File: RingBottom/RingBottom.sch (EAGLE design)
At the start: 28 parts

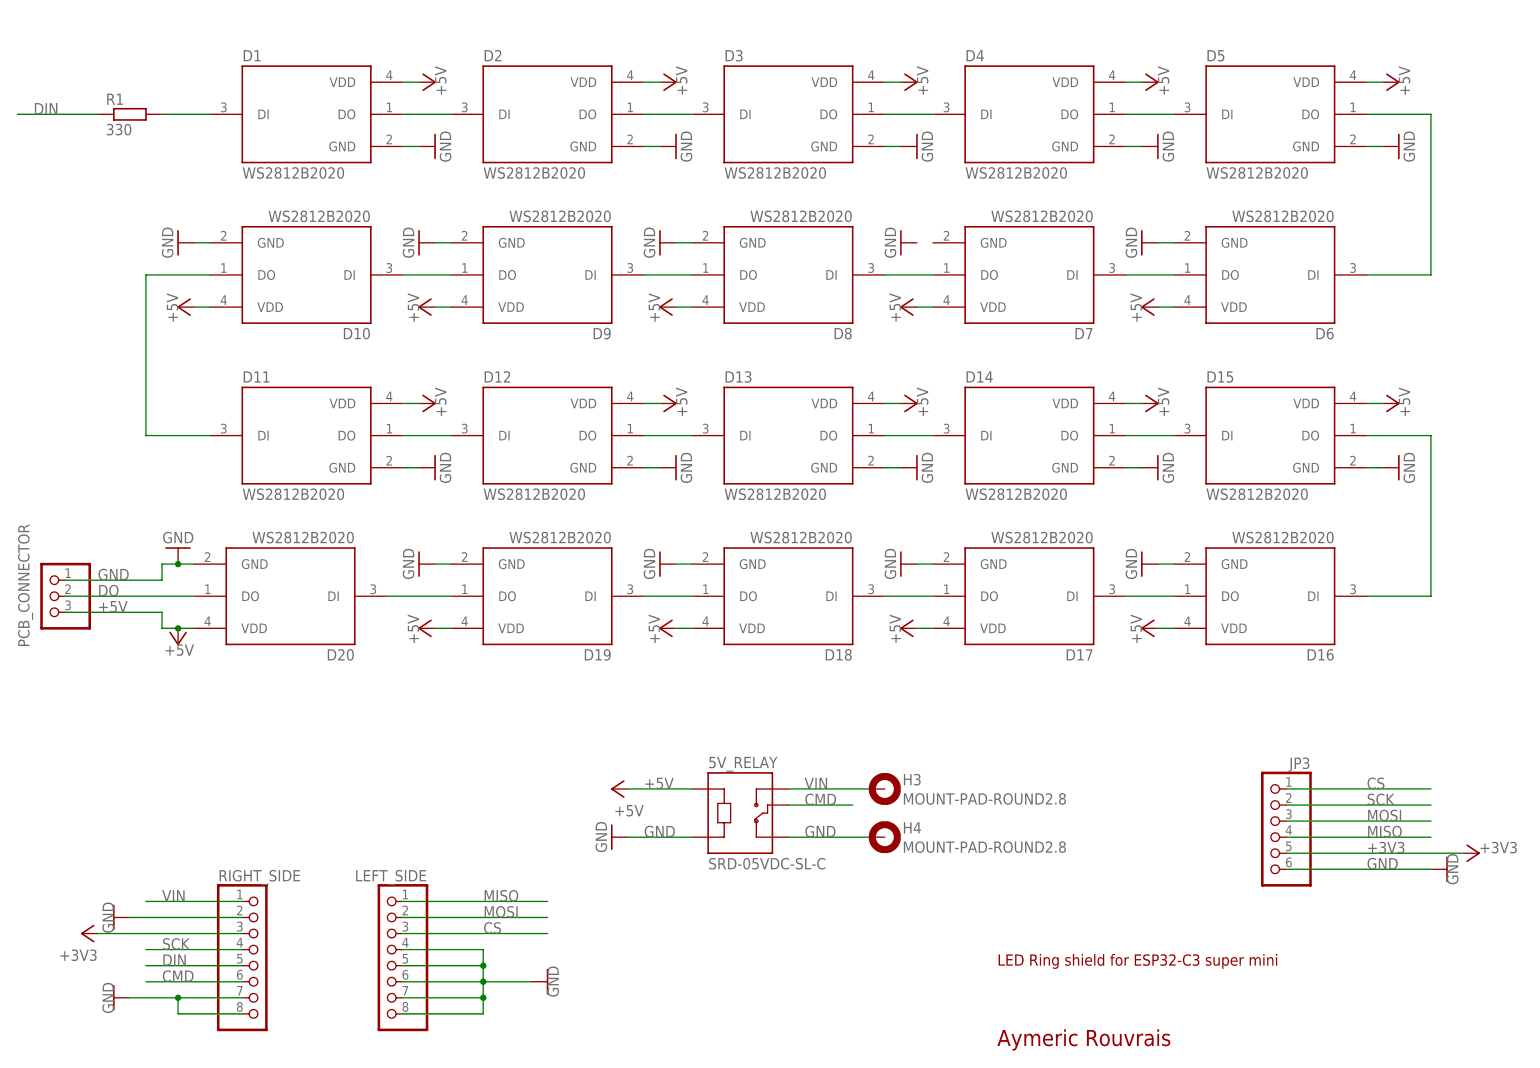
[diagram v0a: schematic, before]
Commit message: V2.0
Now there is a top and bottom PCB. They have the correct dimensions.
The bottom one has the LEDs and the top one has all the rest.
There is still a possibility to integrate a sd card
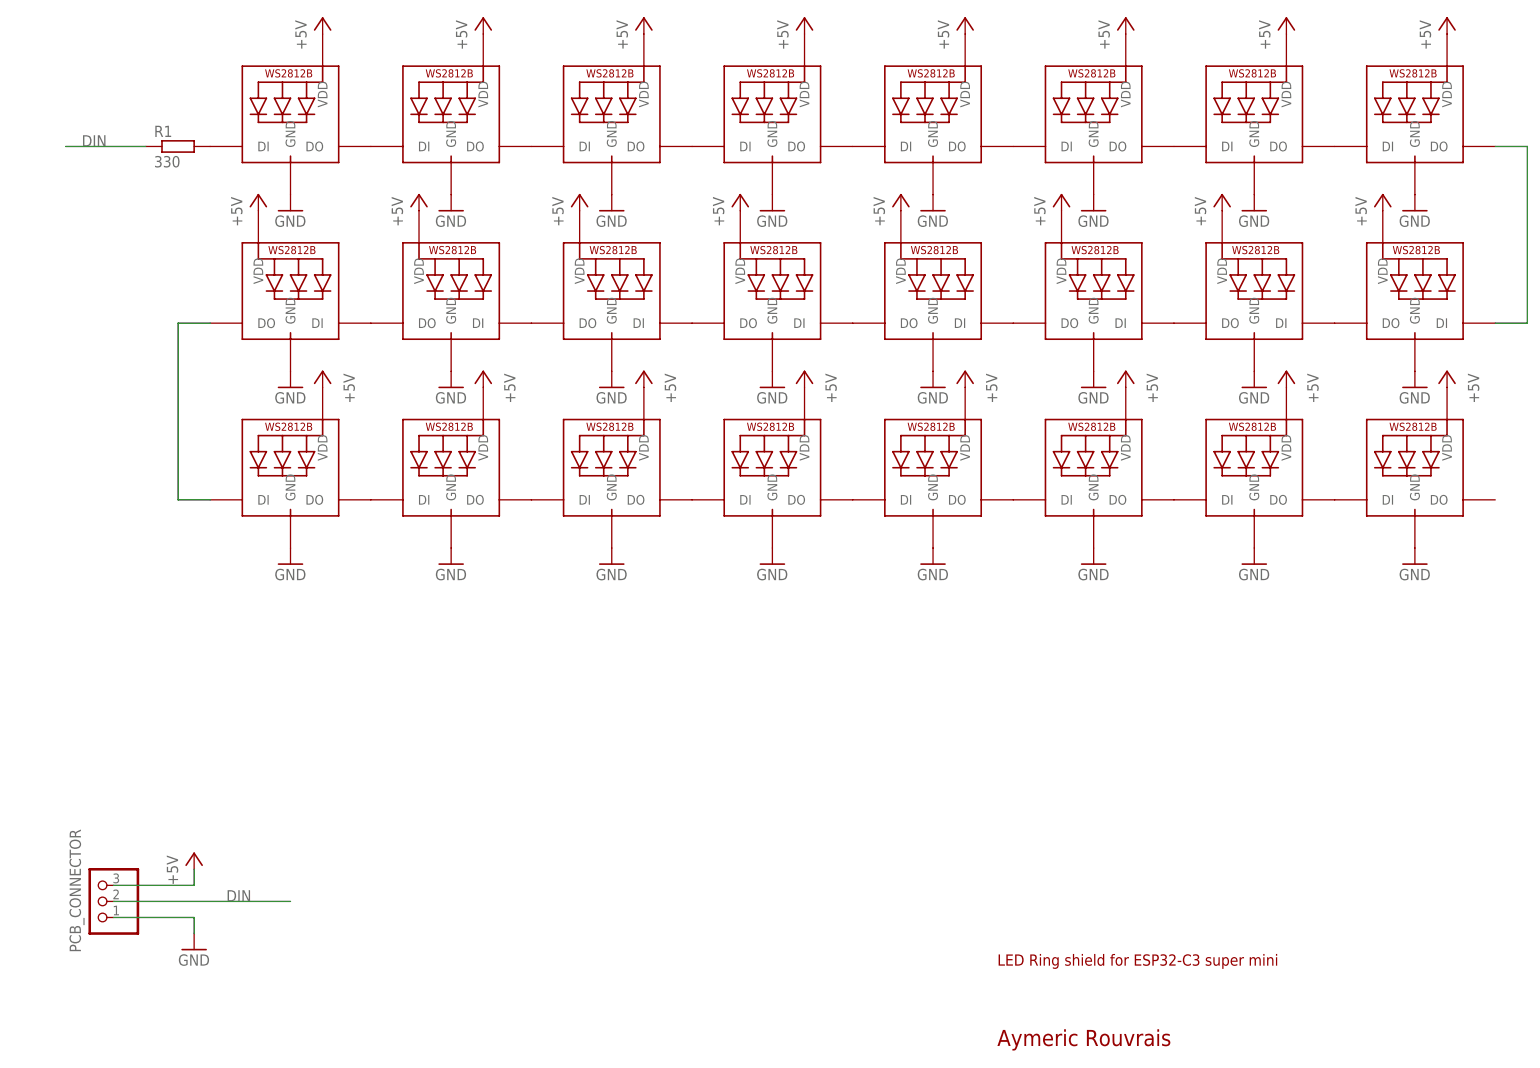
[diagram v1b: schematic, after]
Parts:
- removed 5V_RELAY: SRD-05VDC-SL-C, SRD-05VDC-SL-C:SRD-05VDC-SL-C
- removed D1, D10, D11, D12, D13, D14, D15, D16, D17, D18, D19, D2, D20, D3, D4, D5, D6, D7, D8, D9: WS2812B2020, WS2812B2020:WS2812B2020
- removed H3, H4: MOUNT-PAD-ROUND2.8, holes:MOUNT-PAD-ROUND2.8
- removed JP3: (no value), pinhead:PINHD-1X6/90
- removed LEFT_SIDE, RIGHT_SIDE: (no value), pinhead:PINHD-1X8
- added LED1, LED10, LED11, LED12, LED13, LED14, LED15, LED16, LED17, LED18, LED19, LED2, LED20, LED21, LED22, LED23, LED24, LED3, LED4, LED5, LED6, LED7, LED8, LED9: WS2812B5050, WS2812B:WS2812B5050
- PCB_CONNECTOR: device pinhead:PINHD-1X3/90 -> pinhead:PINHD-1X3
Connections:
- removed net +3V3: JP3.5, RIGHT_SIDE.3
- removed net CMD: 5V_RELAY.COM, RIGHT_SIDE.6
- removed net CS: JP3.1, LEFT_SIDE.3
- removed net DO: D20.DO, PCB_CONNECTOR.2
- removed net MISO: JP3.4, LEFT_SIDE.1
- removed net MOSI: JP3.3, LEFT_SIDE.2
- removed net SCK: JP3.2, RIGHT_SIDE.4
- removed net VIN: 5V_RELAY.NO, H3.MOUNT, RIGHT_SIDE.1
- new net N$18: LED23.DO, LED24.DI
- new net N$23: LED10.DI, LED9.DO
- new net N$24: LED20.DO, LED21.DI
- new net N$8: LED15.DO, LED16.DI
- net +5V: now also LED1.VDD, LED10.VDD, LED11.VDD, LED12.VDD, LED13.VDD, LED14.VDD, LED15.VDD, LED16.VDD, LED17.VDD, LED18.VDD, LED19.VDD, LED2.VDD, LED20.VDD, LED21.VDD, LED22.VDD, LED23.VDD, LED24.VDD, LED3.VDD, LED4.VDD, LED5.VDD, LED6.VDD, LED7.VDD, LED8.VDD, LED9.VDD; no longer 5V_RELAY.A1, D1.VDD, D10.VDD, D11.VDD, D12.VDD, D13.VDD, D14.VDD, D15.VDD, D16.VDD, D17.VDD, D18.VDD, D19.VDD, D2.VDD, D20.VDD, D3.VDD, D4.VDD, D5.VDD, D6.VDD, D7.VDD, D8.VDD, D9.VDD
- net DIN: now also PCB_CONNECTOR.2; no longer RIGHT_SIDE.5
- net GND: now also LED1.GND, LED10.GND, LED11.GND, LED12.GND, LED13.GND, LED14.GND, LED15.GND, LED16.GND, LED17.GND, LED18.GND, LED19.GND, LED2.GND, LED20.GND, LED21.GND, LED22.GND, LED23.GND, LED24.GND, LED3.GND, LED4.GND, LED5.GND, LED6.GND, LED7.GND, LED8.GND, LED9.GND; no longer 5V_RELAY.A2, 5V_RELAY.NC, D1.GND, D10.GND, D11.GND, D12.GND, D13.GND, D14.GND, D15.GND, D16.GND, D17.GND, D18.GND, D19.GND, D2.GND, D20.GND, D3.GND, D4.GND, D5.GND, D6.GND, D8.GND, D9.GND, H4.MOUNT, JP3.6, LEFT_SIDE.4, LEFT_SIDE.5, LEFT_SIDE.6, LEFT_SIDE.7, LEFT_SIDE.8, RIGHT_SIDE.2, RIGHT_SIDE.7, RIGHT_SIDE.8
- net N$1: now also LED1.DO, LED2.DI; no longer D1.DI, R1.2
- net N$10: now also LED4.DO, LED5.DI; no longer D8.DO, D9.DI
- net N$11: now also LED11.DO, LED12.DI; no longer D7.DO, D8.DI
- net N$12: now also LED8.DO, LED9.DI; no longer D6.DO, D7.DI
- net N$13: now also LED17.DO, LED18.DI; no longer D14.DO, D15.DI
- net N$14: now also LED18.DO, LED19.DI; no longer D13.DO, D14.DI
- net N$15: now also LED19.DO, LED20.DI; no longer D12.DO, D13.DI
- net N$16: now also LED5.DO, LED6.DI; no longer D11.DO, D12.DI
- net N$17: now also LED22.DO, LED23.DI; no longer D10.DO, D11.DI
- net N$19: now also LED21.DO, LED22.DI; no longer D17.DO, D18.DI
- net N$2: now also LED2.DO, LED3.DI; no longer D1.DO, D2.DI
- net N$20: now also LED10.DO, LED11.DI; no longer D16.DO, D17.DI
- net N$21: now also LED14.DO, LED15.DI; no longer D15.DO, D16.DI
- net N$22: now also LED13.DO, LED14.DI; no longer D19.DO, D20.DI
- net N$3: now also LED3.DO, LED4.DI; no longer D2.DO, D3.DI
- net N$4: now also LED1.DI, R1.2; no longer D3.DO, D4.DI
- net N$5: now also LED6.DO, LED7.DI; no longer D4.DO, D5.DI
- net N$6: now also LED7.DO, LED8.DI; no longer D5.DO, D6.DI
- net N$7: now also LED16.DO, LED17.DI; no longer D18.DO, D19.DI
- net N$9: now also LED12.DO, LED13.DI; no longer D10.DI, D9.DO
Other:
- note removed: "External power supply"
- moved on the sheet: PCB_CONNECTOR, R1
